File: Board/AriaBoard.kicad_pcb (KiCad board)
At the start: 2 copper layers, 108.7 x 74.9 mm, 64 parts, among them J1 USB_MICRO, J2 HR911105_RJ45, P1 CONN_2, P10 CONN_9, P11 CONN_4, P12 CONN_4, P13 CONN_4, P14 CONN_4, P2 CONN_2, P3 CONN_4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

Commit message: First partial routing
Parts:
- SW1, U2: moved to B.Cu
- moved P7 62.6 mm to (205.2, 131.6)
- moved P2 25.6 mm to (217.4, 194.1)
- moved P4 25.6 mm to (209.8, 194.1)
- moved C9 9.75 mm to (189.2, 189.2), turned to 270 degrees
- moved R1 7.06 mm to (247.1, 190.2)
- moved P9 2.79 mm to (198.4, 148.1)
- moved SW1 0.36 mm to (177.8, 164.6), turned to 90 degrees
- moved C5 0.33 mm to (188.0, 184.2)
- moved U2 0.14 mm to (267.7, 150.4), turned to 270 degrees
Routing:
- net PGND: track 0.00 -> 297.9 mm, vias 0 -> 6
- net /Voltage_regulation_3V/VIN: track 0.00 -> 59.8 mm, vias 0 -> 5
- net /GPIO_96: track 0.00 -> 47.2 mm
- net /vbat: track 0.00 -> 40.2 mm, vias 0 -> 2
- net /GPIO_116: track 0.00 -> 35.5 mm, vias 0 -> 1
- net /GPIO_117: track 0.00 -> 35.3 mm, vias 0 -> 1
- net /GPIO_127: track 0.00 -> 31.0 mm, vias 0 -> 1
- net /GPIO_125: track 0.00 -> 30.8 mm, vias 0 -> 1
- net /Voltage_Regulation_5V/VIN: track 0.00 -> 29.9 mm, vias 0 -> 3
- net /Voltage_Regulation_5V/+5V: track 0.00 -> 27.5 mm, vias 0 -> 2
- net /GPIO_126: track 0.00 -> 26.4 mm, vias 0 -> 1
- net /GPIO_114: track 0.00 -> 26.1 mm
- net /CTS0_ttyS1: track 0.00 -> 26.0 mm
- net /Voltage_regulation_3V/+3V: track 0.00 -> 24.5 mm
- net /RTS0_ttyS1: track 0.00 -> 23.9 mm
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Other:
- net class Default: clearance 0.235 -> 0.25; trace_width 0.235 -> 0.4; via_dia 0.889 -> 1; via_drill 0.635 -> 0.8
- net class gnd added: clearance 0.25, trace_width 0.5, via_dia 1, via_drill 0.8
- net class vcc added: clearance 0.25, trace_width 0.45, via_dia 1, via_drill 0.8
- rule trace_clearance: 0.235 -> 0.25

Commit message: routing in progress
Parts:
- removed R1: 0, SM0603_Resistor
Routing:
- net /5v_usb: track 0.00 -> 141.4 mm, vias 0 -> 2
- net PGND: track 297.9 -> 397.4 mm, vias 6 -> 8
- net DGND: track 18.5 -> 115.5 mm, vias 0 -> 3
- net /rd+: track 0.00 -> 95.9 mm, vias 0 -> 1
- net /3v_aria: track 0.00 -> 85.7 mm, vias 0 -> 2
- net /td+: track 0.00 -> 76.8 mm, vias 0 -> 1
- net /rd-: track 0.00 -> 76.0 mm, vias 0 -> 4
- net /eth_l1: track 0.00 -> 73.8 mm, vias 0 -> 1
- net /eth_l2: track 0.00 -> 71.8 mm, vias 0 -> 1
- net /td-: track 0.00 -> 68.9 mm, vias 0 -> 1
- net /FTDI_Debug_port/RST: track 8.00 -> 74.4 mm, vias 0 -> 4
- net /eth_3v3: track 3.05 -> 68.5 mm, vias 0 -> 1
- net /USB-A_D-: track 0.00 -> 60.5 mm, vias 0 -> 3
- net /USB-A_D+: track 0.00 -> 50.9 mm, vias 0 -> 2
- net /do: track 0.00 -> 43.0 mm, vias 0 -> 1
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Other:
- net class Default: trace_width 0.4 -> 0.35
- net class gnd: trace_width 0.5 -> 0.45

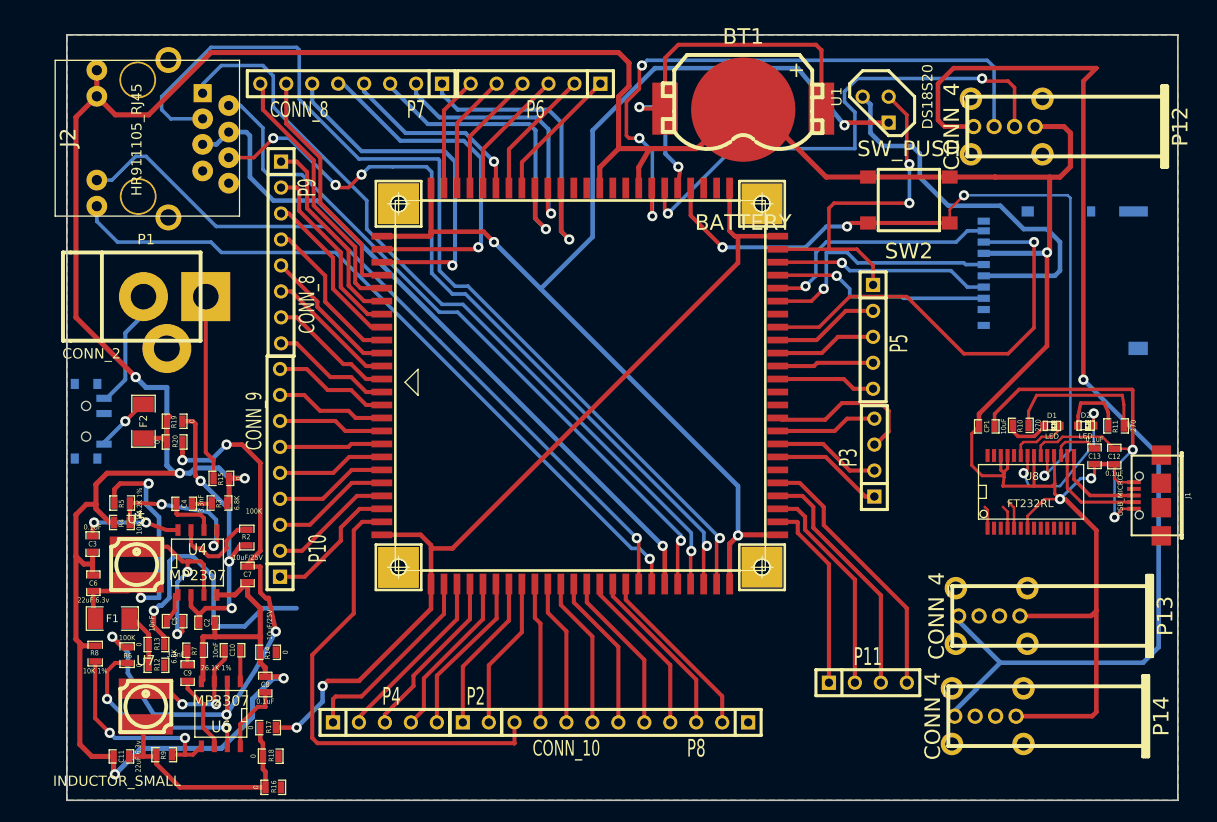
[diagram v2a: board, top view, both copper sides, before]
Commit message: Routing finished! Ready to testing and debug
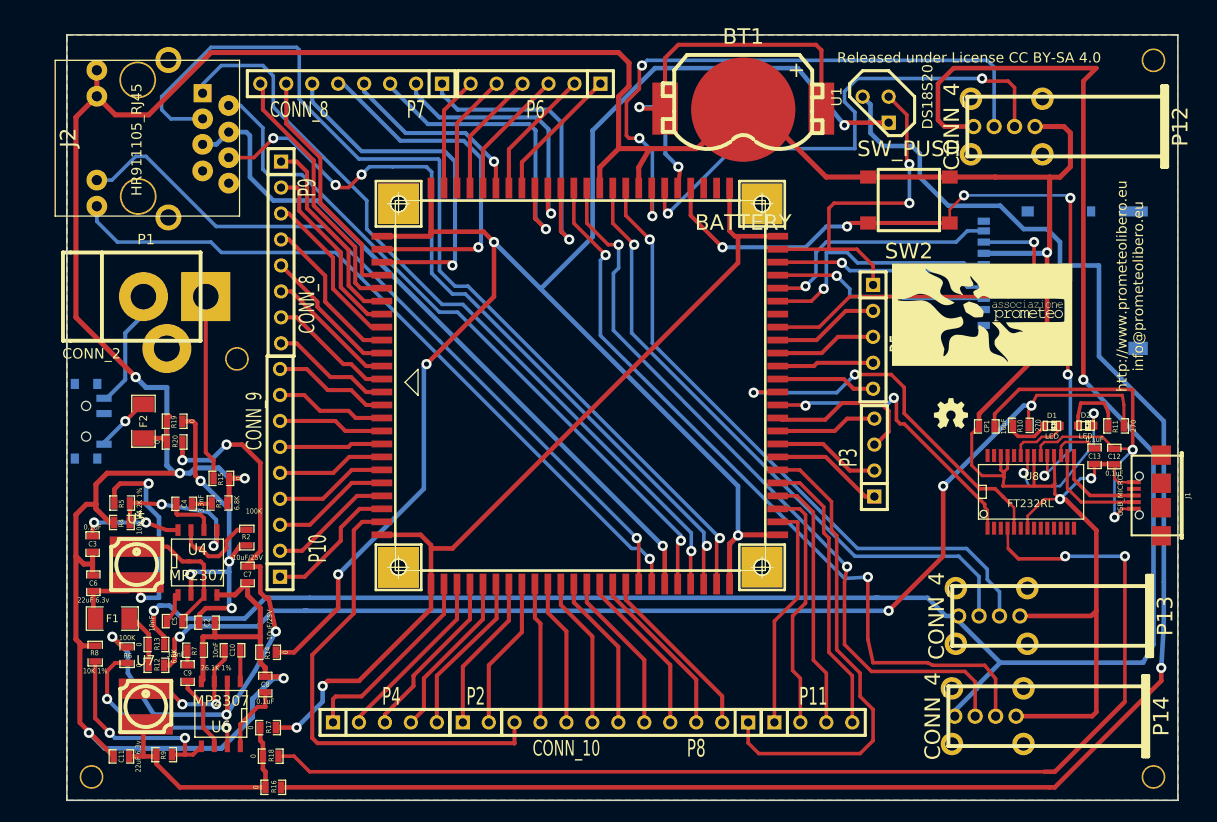
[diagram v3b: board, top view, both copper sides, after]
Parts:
- added G***: OSHW, OSHW, F.Cu at (263.9, 163.8)
- added G***: LOGO, Prometeo_10mm, F.Cu at (267.0, 154.2)
- added MOUNTING_HOLE: VAL**, MOUNTING_HOLE_M2, F.Cu at (179.8, 199.4)
- added MOUNTING_HOLE: VAL**, MOUNTING_HOLE_M2, F.Cu at (283.7, 199.4)
- added MOUNTING_HOLE: VAL**, MOUNTING_HOLE_M2, F.Cu at (283.7, 129.3)
- added MOUNTING_HOLE: VAL**, MOUNTING_HOLE_M2, F.Cu at (194.1, 158.5)
- moved P11 6.60 mm to (250.4, 194.1)
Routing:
- net /3v_ext: track 38.6 -> 176.1 mm, vias 0 -> 1
- net /FTDI_Debug_port/+3V: track 2.27 -> 114.4 mm, vias 0 -> 2
- net /FTDI_Debug_port/+5V: track 14.5 -> 116.1 mm, vias 0 -> 4
- net /USB-C_D+: track 0.00 -> 76.7 mm, vias 0 -> 2
- net /USB-C_D-: track 0.00 -> 73.8 mm, vias 0 -> 2
- net /USB-B_D+: track 0.00 -> 63.3 mm, vias 0 -> 1
- net /USB-B_D-: track 0.00 -> 62.9 mm, vias 0 -> 1
- net /5v_usb: track 141.4 -> 197.5 mm
- net DGND: track 115.5 -> 165.6 mm, vias 3 -> 5
- net /GPIO_36: track 0.00 -> 46.8 mm
- net /FTDI_Debug_port/D_RXD: track 2.83 -> 37.9 mm, vias 0 -> 2
- net /FTDI_Debug_port/D_TXD: track 2.20 -> 28.5 mm, vias 0 -> 2
- net /do: track 43.0 -> 36.4 mm
- net N-00000117: track 19.4 -> 13.7 mm, vias 2 -> 0
- net /Voltage_Regulation_5V/VIN: track 29.9 -> 33.6 mm, vias 3 -> 4
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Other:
- board text added: "Released under License CC BY-SA 4.0"
- board text added: "http://www.prometeolibero.eu info@prometeolibero.eu"
